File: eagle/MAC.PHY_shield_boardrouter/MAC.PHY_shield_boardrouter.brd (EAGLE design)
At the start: 100 x 80 mm, 21 parts, among them IC1 ENC28J60SP, Q1 CSM-7X-DU

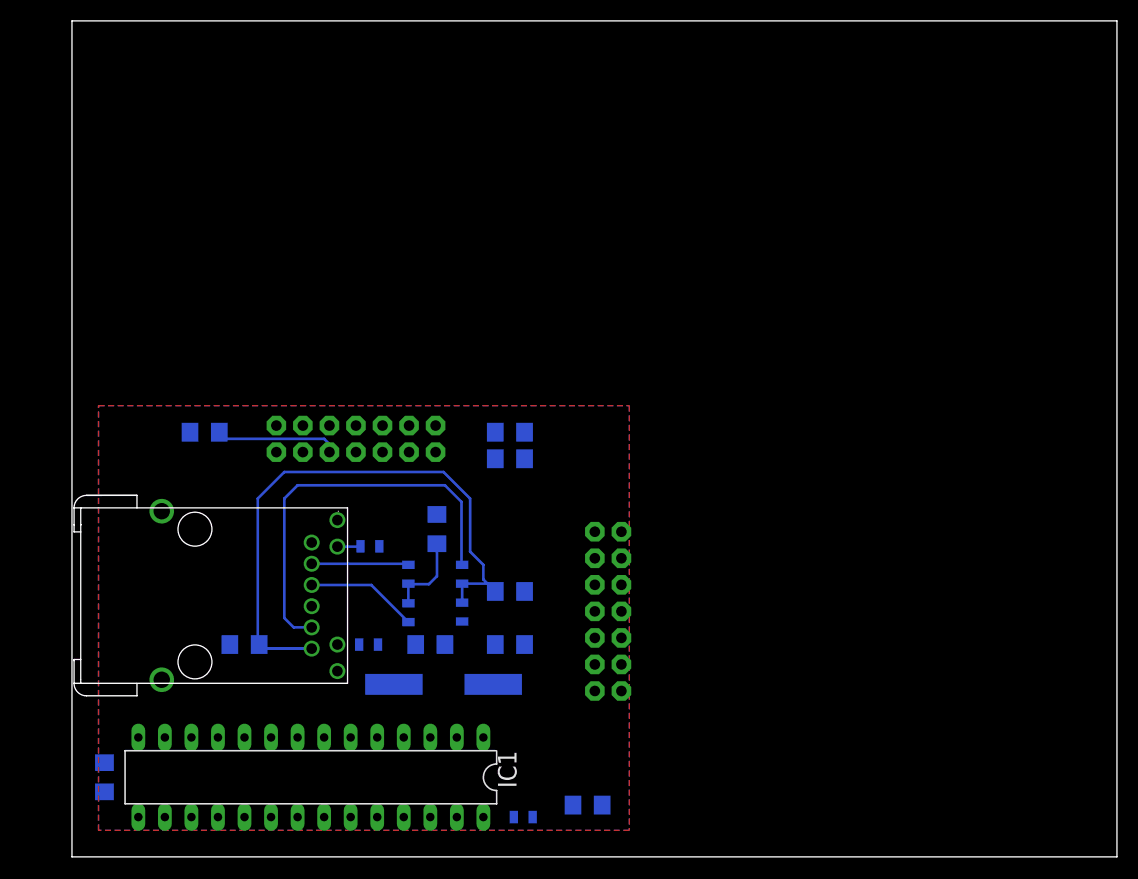
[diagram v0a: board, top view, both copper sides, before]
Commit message: Finished the PDIP dev board for the enc28J60
Signed-off-by: Pavlo Manovi <pavlo.manovi@gmail.com>
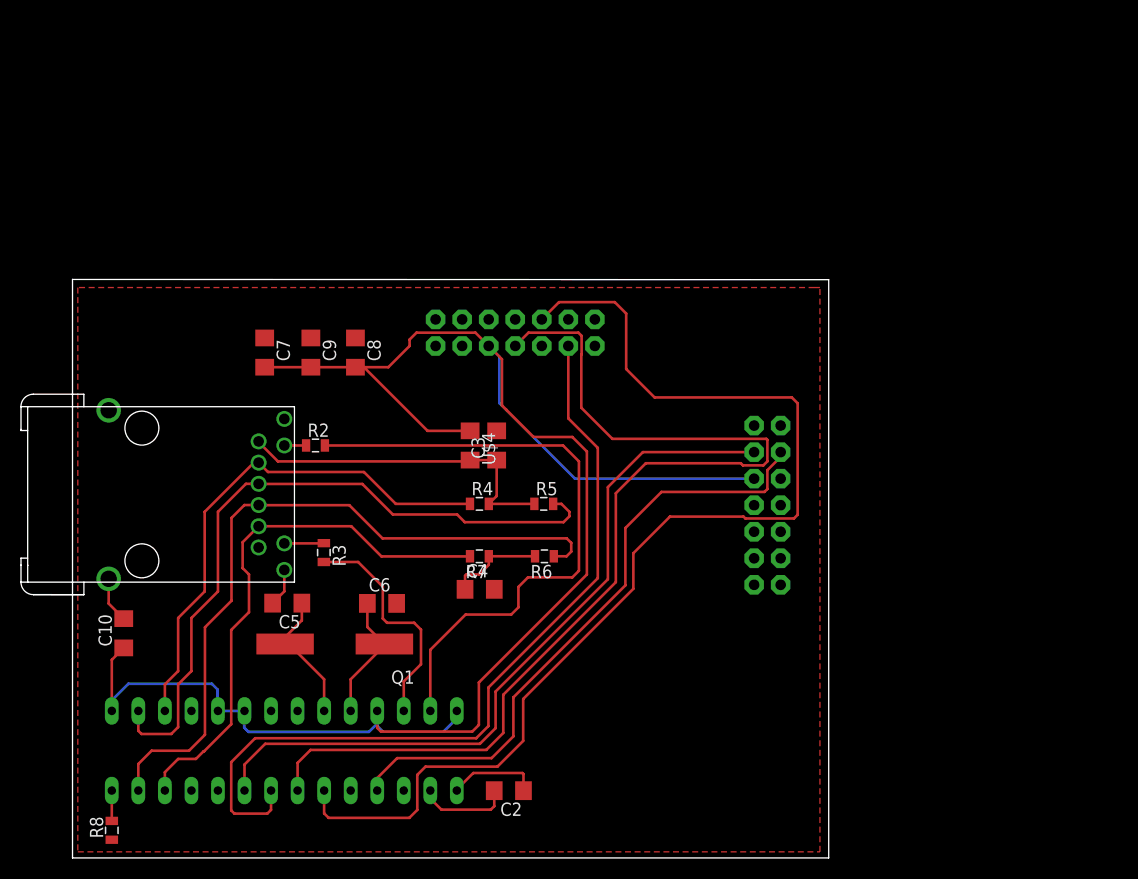
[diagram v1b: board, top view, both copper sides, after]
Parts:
- moved C10 47.3 mm to (4.95, 21.4), flipped to the top, turned to 90 degrees
- moved R8 39.4 mm to (3.81, 2.54), flipped to the top, turned to 90 degrees
- moved C2 38.7 mm to (41.8, 6.34), flipped to the top, turned to 180 degrees
- moved U$4 28.8 mm to (38.1, 39.4), flipped to the top, turned to 270 degrees
- moved C7 24.7 mm to (18.4, 48.3), flipped to the top, turned to 270 degrees
- moved U$3 24.7 mm to (20.3, 41.9), flipped to the bottom, turned to 270 degrees
- moved R2 19.7 mm to (23.3, 39.4), flipped to the top, turned to 0 degrees
- moved U$1 18.3 mm to (20.3, 17.8)
- moved C8 17.9 mm to (27.1, 48.3), flipped to the top, turned to 270 degrees
- moved C5 14.3 mm to (20.6, 24.3), flipped to the top
- moved R6 14.1 mm to (45.2, 28.8), flipped to the top, turned to 180 degrees
- moved C3 14.0 mm to (40.6, 39.4), flipped to the top, turned to 90 degrees
- moved R5 13.0 mm to (45.1, 33.8), flipped to the top, turned to 0 degrees
- moved C6 12.9 mm to (29.7, 24.3), flipped to the top, turned to 0 degrees
- moved C9 12.7 mm to (22.9, 48.3), flipped to the top, turned to 270 degrees
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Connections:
- net VCC3V3: now also IC1.28
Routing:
- net VCC3V3: track 11.8 -> 177.7 mm
- net N$15: track 0.00 -> 109.1 mm
- net N$16: track 0.00 -> 101.9 mm
- net N$12: track 0.00 -> 78.5 mm
- net N$10: track 0.00 -> 70.9 mm
- net N$6: track 0.00 -> 67.1 mm
- net N$2: track 0.00 -> 59.8 mm
- net N$17: track 0.00 -> 59.4 mm
- net N$7: track 10.7 -> 69.1 mm
- net N$9: track 9.30 -> 52.0 mm
- net N$4: track 62.1 -> 32.5 mm
- net N$3: track 0.00 -> 22.2 mm
- net GND: track 0.00 -> 17.0 mm
- net N$13: track 0.00 -> 12.7 mm
- net N$14: track 0.00 -> 12.3 mm
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- added copper zone on layer 1, net GND
- removed copper zone on layer 16, net GND
- removed copper zone on layer 1, net VCC3V3
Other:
- board size 100 x 80 mm -> 72.4 x 55.4 mm
